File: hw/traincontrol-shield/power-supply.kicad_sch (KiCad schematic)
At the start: 9 parts, among them U1 MP2359DJ

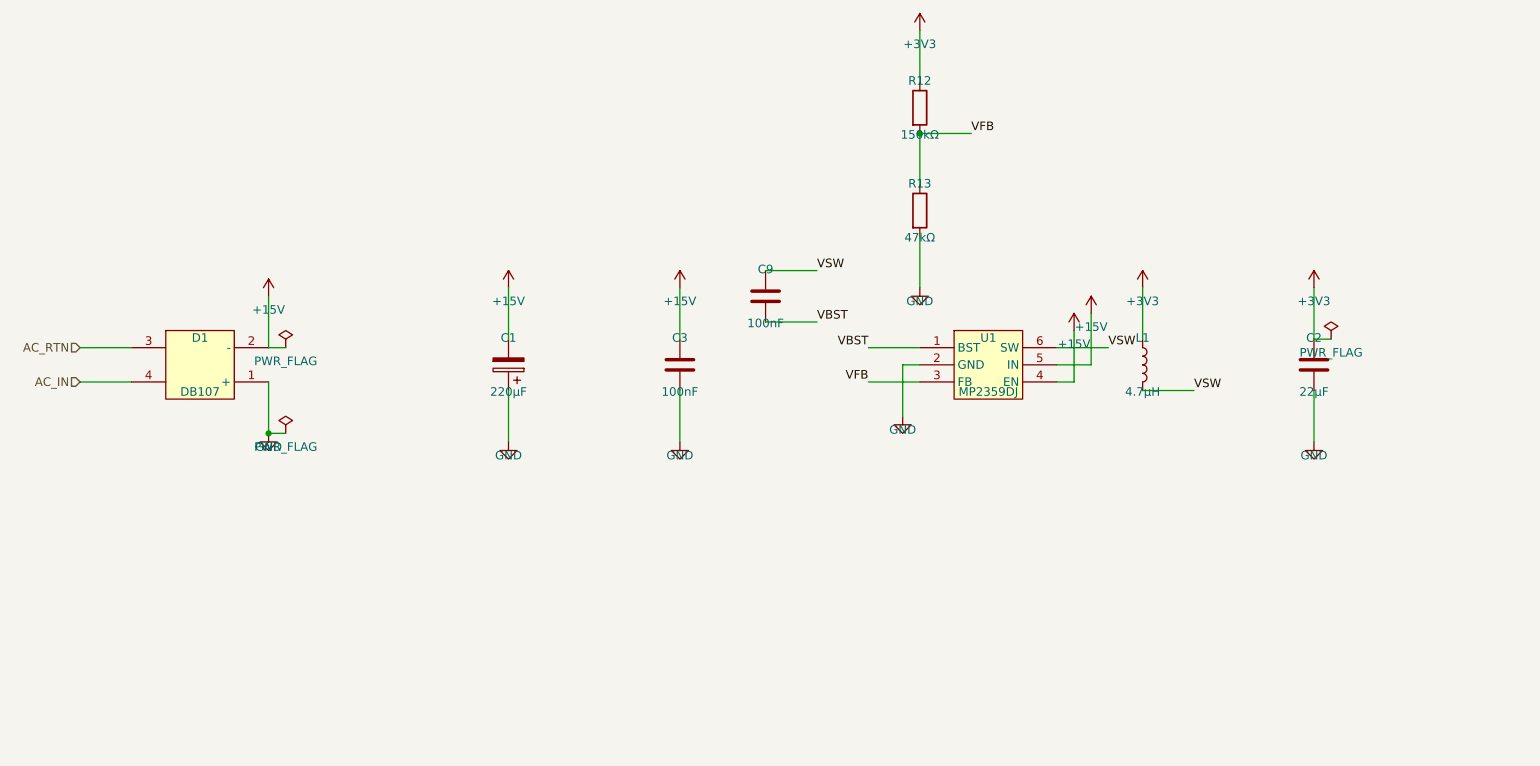
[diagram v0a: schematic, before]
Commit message: Schematic updates by hand.
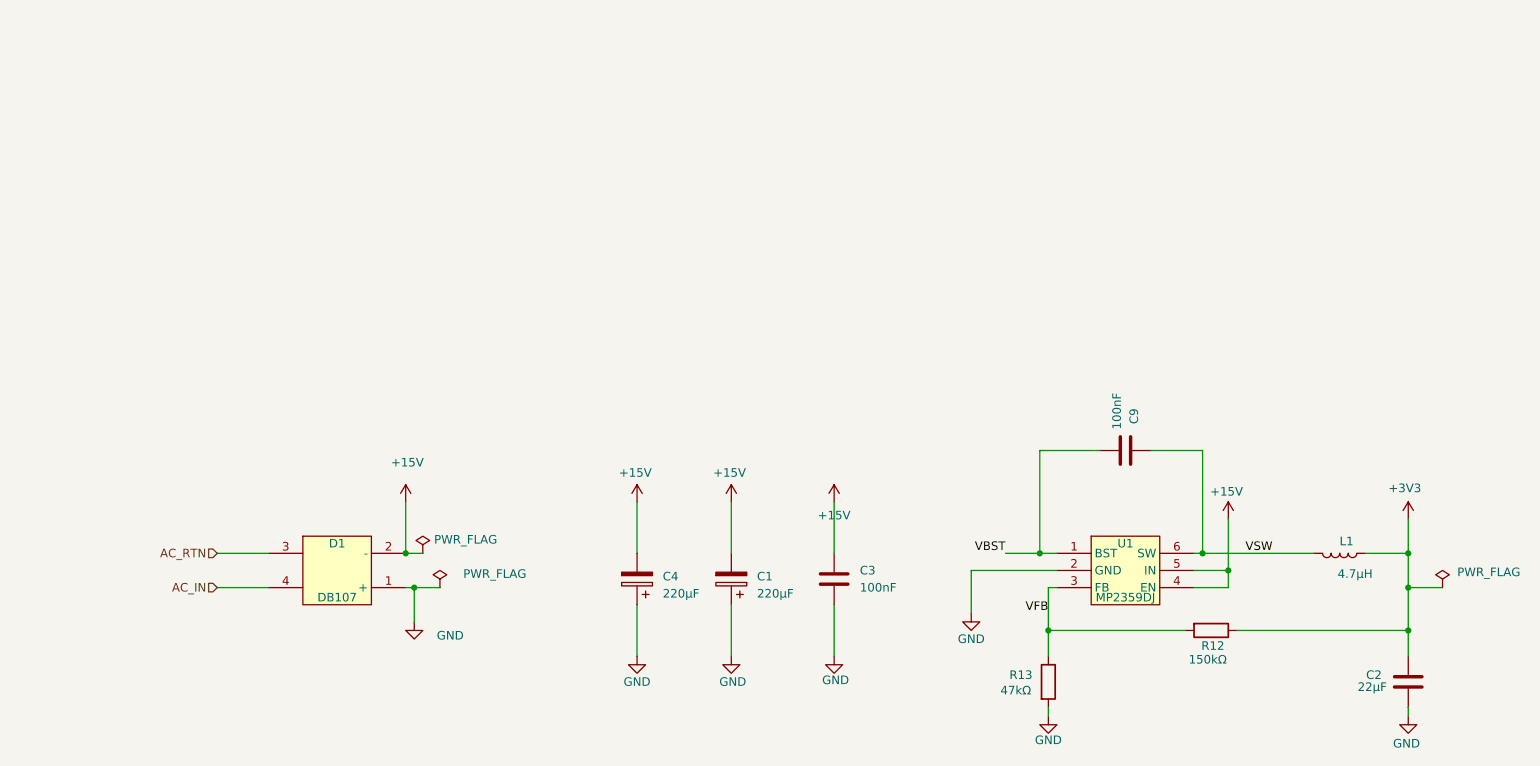
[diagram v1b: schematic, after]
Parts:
- added C4: 220µF, Capacitor_SMD:CP_Elec_6.3x7.7, symbol Device:C_Polarized
- C1: footprint Capacitor_THT:CP_Radial_D8.0mm_P3.50mm -> Capacitor_SMD:CP_Elec_6.3x7.7
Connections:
- net +15V: now also C4.2
- net GND: now also C4.1
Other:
- moved on the sheet: C1, C2, C3, C9, D1, L1, R12, R13, U1
